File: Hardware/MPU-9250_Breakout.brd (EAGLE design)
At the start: 17 x 17.8 mm, 18 parts, among them U1 MPU-9250

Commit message: Loaded up new DRC
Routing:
- net GND: track 2.60 -> 4.30 mm, vias 7 -> 9
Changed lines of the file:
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@@
 <?xml version="1.0" encoding="utf-8"?>
 <!DOCTYPE eagle SYSTEM "eagle.dtd">
-<eagle version="7.2.0">
+<eagle version="7.4.0">
 <drawing>
 <settings>
@@
 </class>
 </classes>
-<designrules name="Gold_Phoenix_Standard_Spec_2_layer">
-<description language="en">&lt;b&gt;EAGLE Design Rules&lt;/b&gt;
+<designrules name="SparkFun-2-layer-FAB-LIMIT">
+<description language="en">&lt;b&gt;SparkFun 2 Layer Design Rule Checks - STANDARD/TIGHT/FAB-LIMIT&lt;/b&gt;
 &lt;p&gt;
-The default Design Rules have been set to cover
-a wide range of applications. Your particular design
-may have different requirements, so please make the
-necessary adjustments and save your customized
-design rules under a new name.</description>
+These rules have been curated by SparkFuns DFM commitee. After doing much research, communicating with our multiple fab houses, and getting quotes of various designs, we have compiled three DRU files.
+&lt;p&gt;
+&lt;b&gt;STANDARD:&lt;/b&gt; This is more of a &quot;best case scenario&quot; set of limitations. If your design has the space, and/or you have the time to work within these parameters, please do. Larger trace width and clearance makes for easier visual inspection of the PCB while troubleshooting (useful in production and to the end user). It also allows for better ability to hack a trace (if you are crazy enough to scrape away the mask and solder to a trace). Another thing to keep in mind is that more metal is just more robust.
+&lt;p&gt;
+&lt;b&gt;TIGHT:&lt;/b&gt; This is where cost comes into play. We have found that most fab houses begin to add extra charges when you go smaller than these specs. In some cases, going to less than 15 mil trace can increase the cost by 10%. (This is why we have set the min drill on this DRU to 15 mil) Same story for traces thinner than 7 mil. To avoid those extra charges, then stay within the rules of this DRU.
+&lt;p&gt;
+&lt;b&gt;FAB-LIMIT:&lt;/b&gt; These set of rules are at the very limit of most fab houses capabilities. You will pay more for these specs, and it should be used on designs that have a darned good reason to need 4 mil vias and 4 mil traces.
+&lt;p&gt;
+**NOTE Clearance, Distance, Sizes, and Restring are all set to different limits in each of these three DRU files. Please compare the files within the CAM job editor window of eagle to see all the numbers.
+&lt;p&gt;
+***NOTE, Please set your Net Classes to default (0mil for all settings), so that it won't effect the DRC when you run it with these settings.</description>
 <param name="layerSetup" value="(1*16)"/>
 <param name="mtCopper" value="0.035mm 0.035mm 0.035mm 0.035mm 0.035mm 0.035mm 0.035mm 0.035mm 0.035mm 0.035mm 0.035mm 0.035mm 0.035mm 0.035mm 0.035mm 0.035mm"/>
 <param name="mtIsolate" value="1.5mm 0.15mm 0.2mm 0.15mm 0.2mm 0.15mm 0.2mm 0.15mm 0.2mm 0.15mm 0.2mm 0.15mm 0.2mm 0.15mm 0.2mm"/>
-<param name="mdWireWire" value="5mil"/>
-<param name="mdWirePad" value="5mil"/>
-<param name="mdWireVia" value="5mil"/>
-<param name="mdPadPad" value="5mil"/>
-<param name="mdPadVia" value="5mil"/>
-<param name="mdViaVia" value="5mil"/>
-<param name="mdSmdPad" value="5mil"/>
-<param name="mdSmdVia" value="5mil"/>
-<param name="mdSmdSmd" value="5mil"/>
+<param name="mdWireWire" value="4mil"/>
+<param name="mdWirePad" value="4mil"/>
+<param name="mdWireVia" value="4mil"/>
+<param name="mdPadPad" value="4mil"/>
+<param name="mdPadVia" value="4mil"/>
+<param name="mdViaVia" value="4mil"/>
+<param name="mdSmdPad" value="4mil"/>
+<param name="mdSmdVia" value="4mil"/>
+<param name="mdSmdSmd" value="4mil"/>
 <param name="mdViaViaSameLayer" value="8mil"/>
 <param name="mnLayersViaInSmd" value="2"/>
-<param name="mdCopperDimension" value="8mil"/>
-<param name="mdDrill" value="8mil"/>
+<param name="mdCopperDimension" value="4mil"/>
+<param name="mdDrill" value="4mil"/>
 <param name="mdSmdStop" value="0mil"/>
-<param name="msWidth" value="5mil"/>
+<param name="msWidth" value="4mil"/>
 <param name="msDrill" value="6mil"/>
 <param name="msMicroVia" value="9.99mm"/>
@@
 <param name="srMinRoundness" value="0mil"/>
 <param name="srMaxRoundness" value="0mil"/>
-<param name="slThermalIsolate" value="5mil"/>
+<param name="slThermalIsolate" value="10mil"/>
 <param name="slThermalsForVias" value="0"/>
 <param name="dpMaxLengthDifference" value="10mm"/>
@@
 <via x="1.143" y="2.6924" extent="1-16" drill="0.381"/>
 <wire x1="4.1656" y1="8.89" x2="4.5466" y2="8.89" width="0.254" layer="1"/>
+<wire x1="6.0966" y1="9.89" x2="7.493" y2="9.89" width="0.254" layer="1"/>
+<wire x1="7.493" y1="9.89" x2="7.493" y2="9.5876" width="0.254" layer="1"/>
+<via x="8.3566" y="15.24" extent="1-16" drill="0.381"/>
+<via x="5.8166" y="15.24" extent="1-16" drill="0.381"/>
 </signal>
 <signal name="VDD">

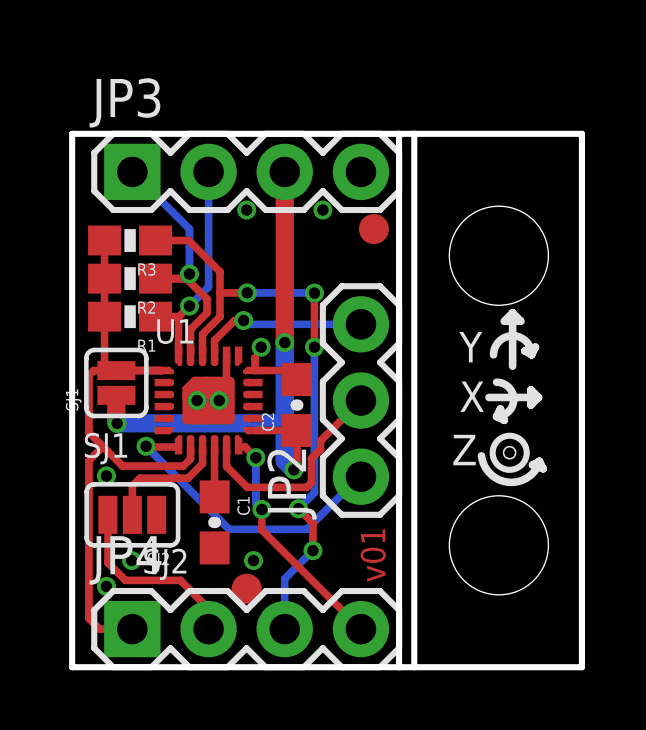
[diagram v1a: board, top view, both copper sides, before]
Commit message: Added mag axes
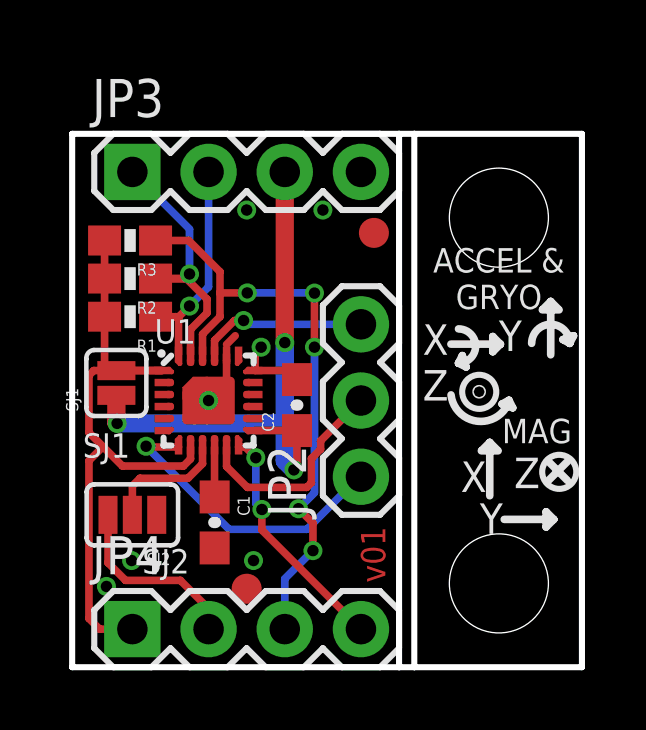
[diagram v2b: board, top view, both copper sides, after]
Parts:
- moved LOGO2 1.90 mm to (14.2, 10.4)
- moved STANDOFF2 1.27 mm to (14.2, 15.0)
- moved STANDOFF1 1.27 mm to (14.2, 2.79)
- moved FID1 0.13 mm to (10.1, 14.5)
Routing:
- net GND: track 4.30 -> 5.03 mm, vias 9 -> 7
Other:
- board text added: "A&G"
- board text added: "ACCEL & GRYO"
- board text added: "MAG"

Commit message: Fixed silk and info
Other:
- board text added: "MPU-9250 BREAKOUT"
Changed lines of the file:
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@@
 SDO</text>
 <text x="2.0066" y="2.5146" size="0.8128" layer="22" font="vector" ratio="15" rot="SMR90" align="center-left">VDDIO</text>
-<text x="2.3368" y="3.937" size="0.8128" layer="21" font="vector" ratio="15" align="top-left">SJ2</text>
-<text x="0.3556" y="7.7978" size="0.8128" layer="21" font="vector" ratio="15" align="top-left">SJ1</text>
+<text x="2.3368" y="3.81" size="0.6096" layer="21" font="vector" ratio="15" align="top-left">SJ2</text>
+<text x="0.3556" y="7.7978" size="0.6096" layer="21" font="vector" ratio="15" align="top-left">SJ1</text>
 <wire x1="1.8542" y1="9.1694" x2="0.5842" y2="9.1694" width="0.254" layer="22"/>
 <wire x1="1.4224" y1="9.6774" x2="1.4224" y2="8.5344" width="0.254" layer="22" curve="180"/>
@@
 <wire x1="15.875" y1="6.223" x2="16.51" y2="6.858" width="0.254" layer="21"/>
 <text x="2.413" y="12.4714" size="0.8128" layer="22" font="vector" ratio="15" rot="SMR0" align="center-left">A&amp;G</text>
+<text x="6.731" y="13.716" size="0.6096" layer="21" font="vector" ratio="15" align="center">MPU-9250
+BREAKOUT</text>
 </plain>
 <attributes>
@@
 <elements>
 <element name="FRAME1" library="SparkFun-Aesthetics" package="CREATIVE_COMMONS" value="FRAME-LETTER" x="-21.8694" y="-13.4112"/>
-<element name="U1" library="Testing" package="QFN24_PAD" value="MPU-9250" x="4.5466" y="8.89"/>
+<element name="U1" library="Testing" package="QFN24_PAD" value="MPU-9250" x="4.5466" y="8.89">
+<attribute name="PROD_ID" value="IC-13192" x="4.5466" y="8.89" size="1.778" layer="27" display="off"/>
+</element>
 <element name="SJ1" library="SparkFun-Passives" package="PAD-JUMPER-2-NC_BY_PASTE_YES_SILK_FULL_BOX" value="JUMPER-PAD-2-NC_BY_PASTEFULL-BOX-SILK" x="1.4732" y="9.4742" rot="R90"/>
 <element name="C1" library="SparkFun-Capacitors" package="0603-CAP" value="0.1uF" x="4.7498" y="4.826" rot="R270">

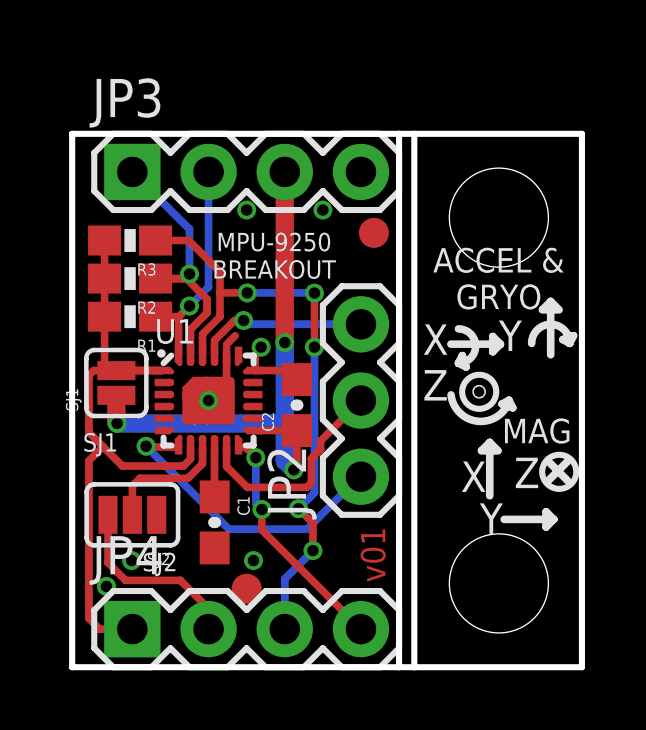
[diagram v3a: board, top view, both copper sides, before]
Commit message: Added stubs to NC pads on main IC and moved silk
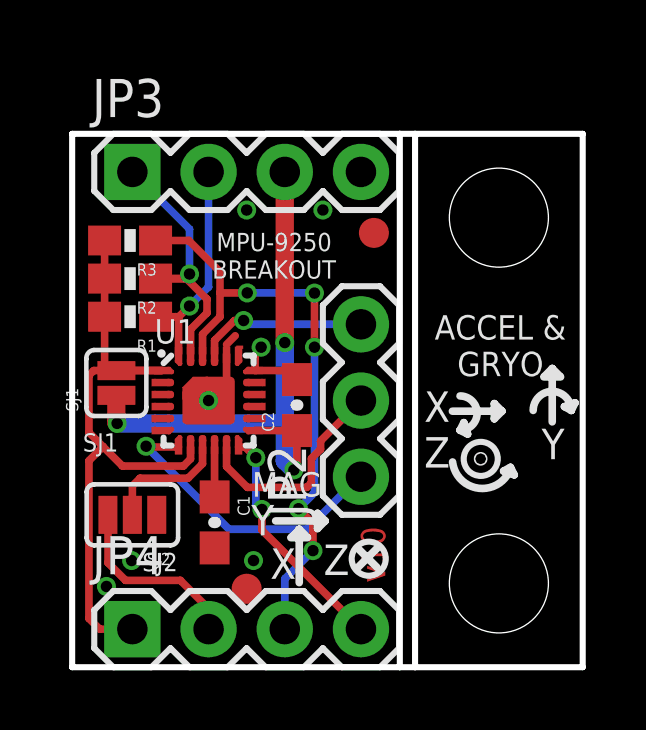
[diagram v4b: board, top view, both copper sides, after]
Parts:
- moved LOGO1 11.9 mm to (15.2, 5.08)
